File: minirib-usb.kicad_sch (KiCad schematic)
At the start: 53 parts, among them J1 USB_B_Micro, J2 SB9600 Out, Q1 MMST3904-7-F, Q2 MMST3906-7-F, Q3 MMST3906-7-F, Q4 MMST3904-7-F, Q5 MMST3904-7-F, Q6 MMST3904-7-F, Q7 MMST3904-7-F, Q8 MMST3906-7-F, Q9 MMST3906-7-F, U1 CH340G, U2 MCP6491T-E, Y1 12MHz

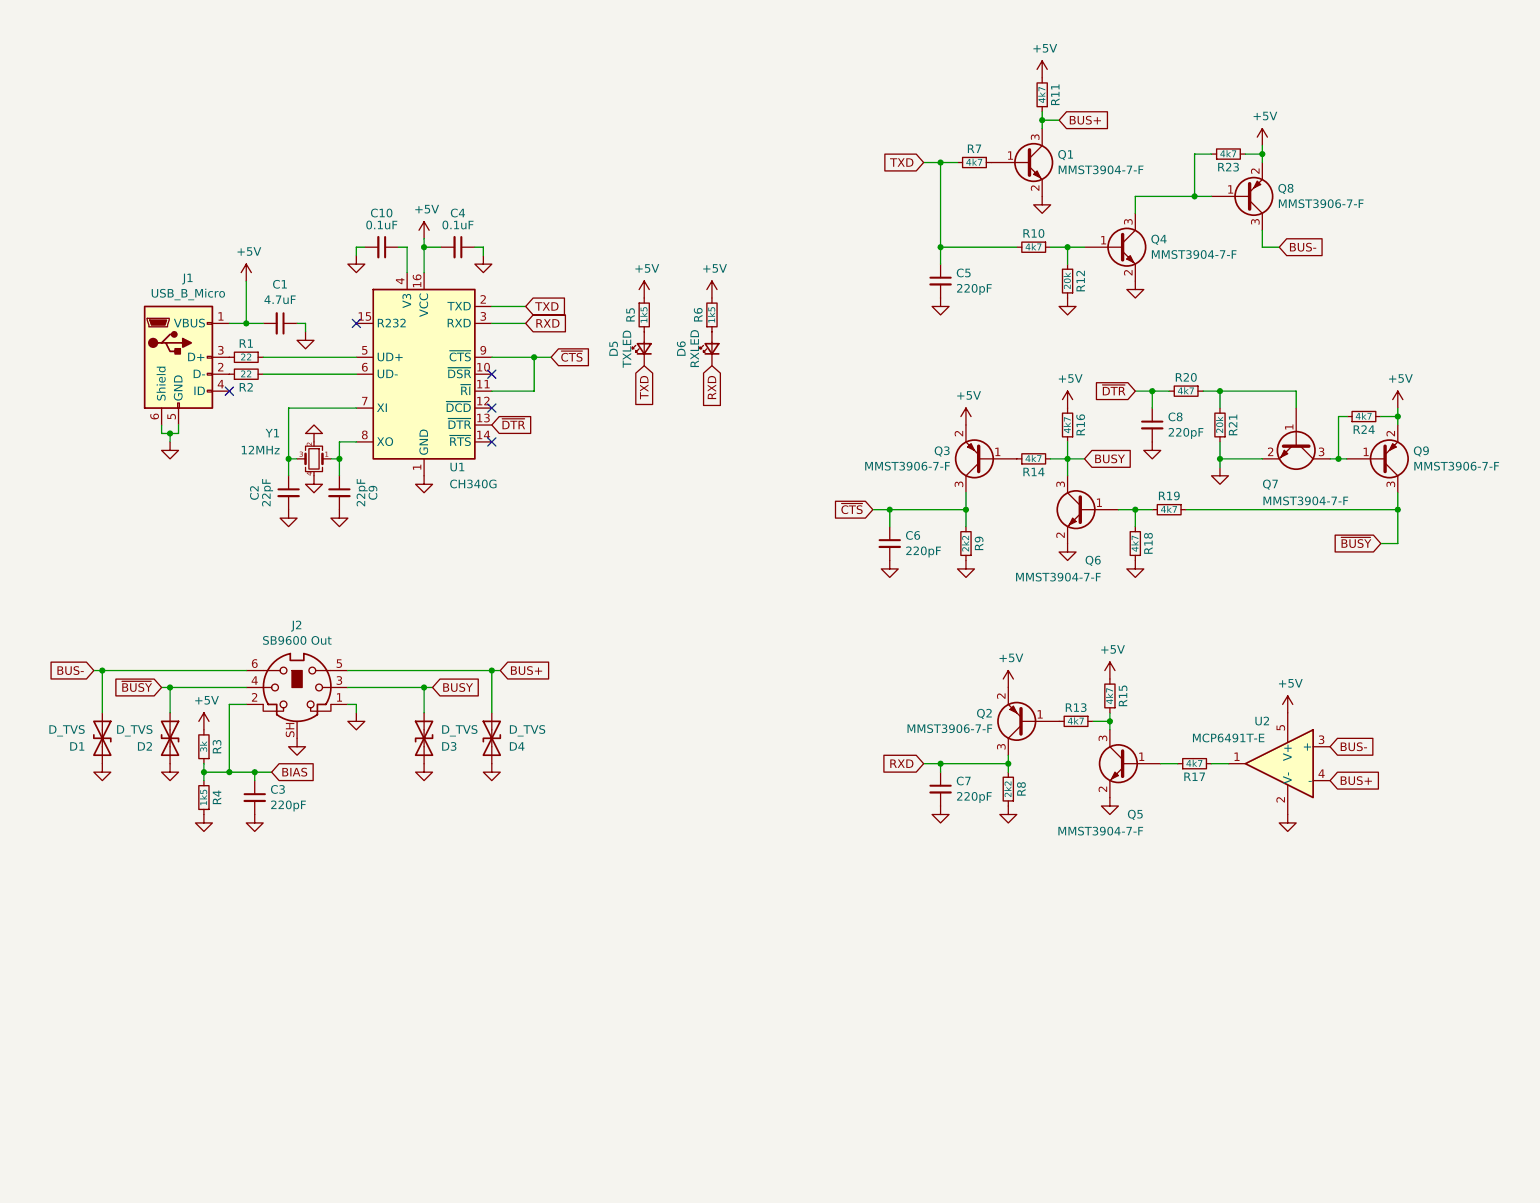
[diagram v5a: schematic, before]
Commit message: rev C total redesign
Changed circuit to use an FT231 + MAX232 usb chain, with original transistor logic conversion identical to the RLN4008B schematic to ensure proper operation
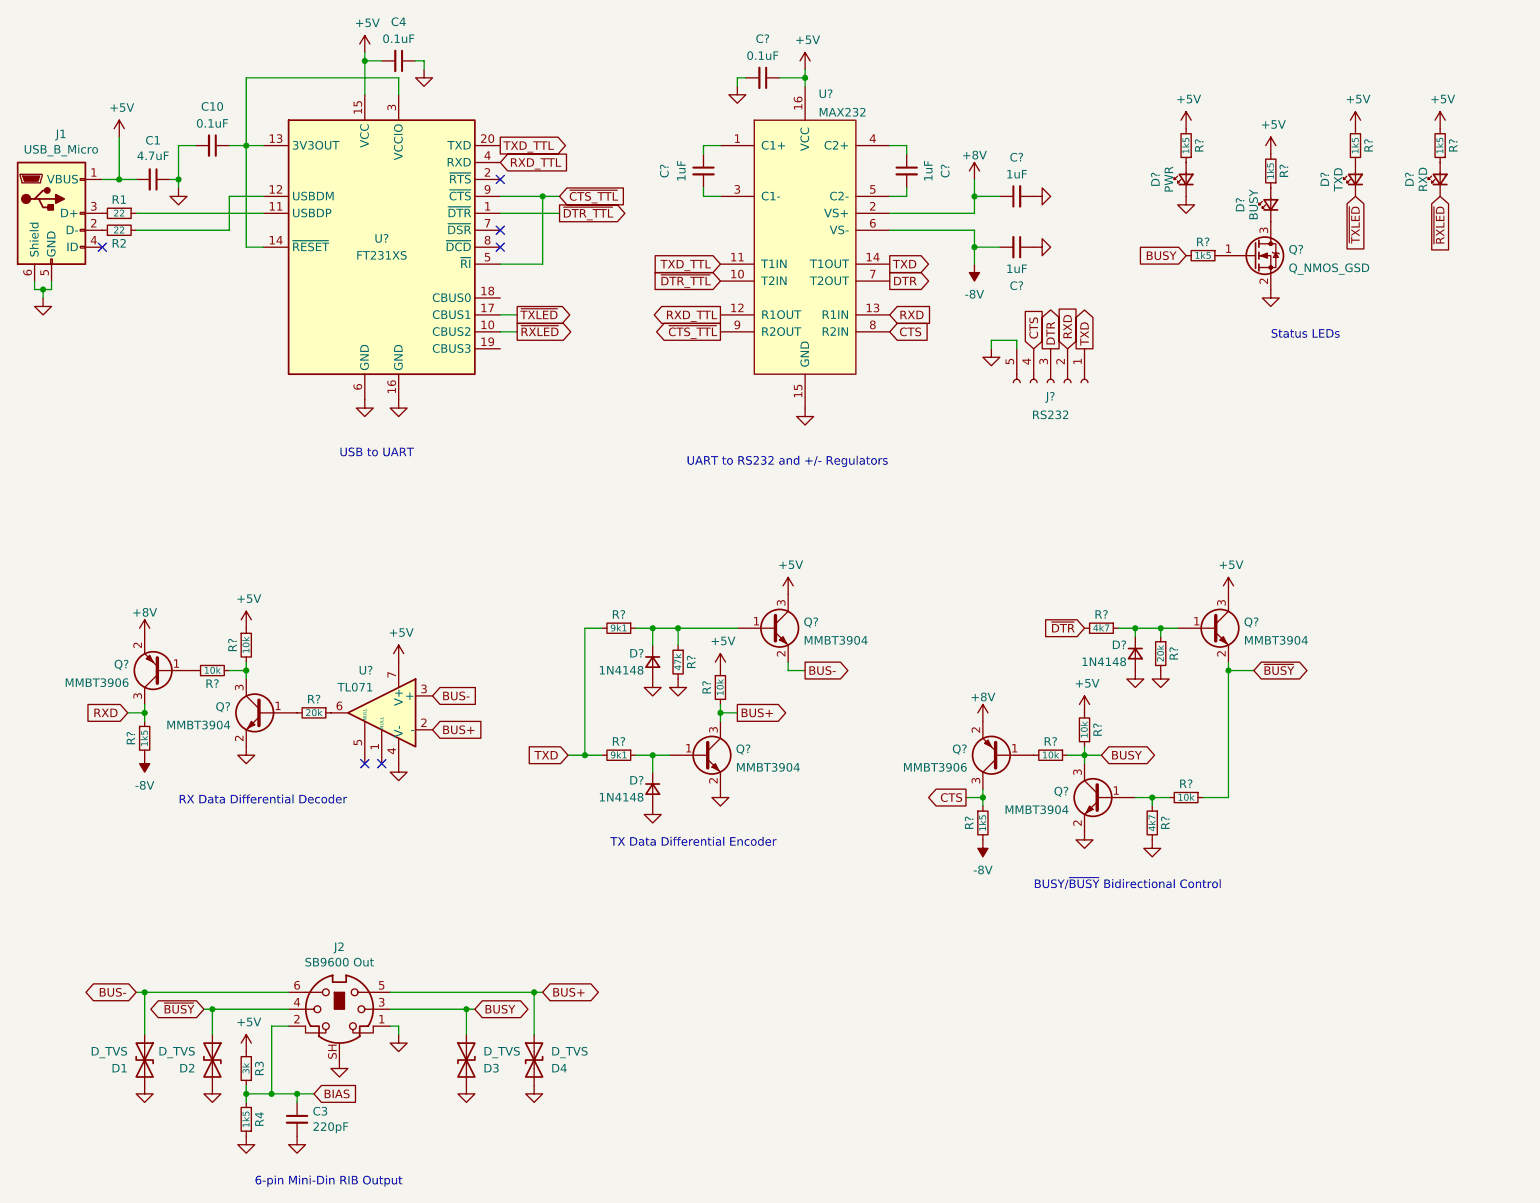
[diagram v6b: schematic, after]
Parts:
- removed C2, C9: 22pF, Capacitor_SMD:C_0805_2012Metric_Pad1.18x1.45mm_HandSolder, symbol Device:C_Small
- removed C5, C6, C7, C8: 220pF, Capacitor_SMD:C_0805_2012Metric_Pad1.18x1.45mm_HandSolder, symbol Device:C_Small
- removed D5: TXLED, Diode_SMD:D_0805_2012Metric_Pad1.15x1.40mm_HandSolder, symbol Device:LED_Small
- removed D6: RXLED, Diode_SMD:D_0805_2012Metric_Pad1.15x1.40mm_HandSolder, symbol Device:LED_Small
- removed Q1, Q4, Q5, Q6, Q7: MMST3904-7-F, Package_TO_SOT_SMD:SOT-323_SC-70_Handsoldering, symbol Device:Q_NPN_BEC
- removed Q2, Q3, Q8, Q9: MMST3906-7-F, Package_TO_SOT_SMD:SOT-323_SC-70_Handsoldering, symbol Device:Q_PNP_BEC
- removed R10, R11, R13, R14, R15, R16, R17, R18, R19, R20, R23, R24, R7: 4k7, Resistor_SMD:R_0805_2012Metric_Pad1.20x1.40mm_HandSolder, symbol Device:R_Small
- removed R12, R21: 20k, Resistor_SMD:R_0805_2012Metric_Pad1.20x1.40mm_HandSolder, symbol Device:R_Small
- removed R5, R6: 1k5, Resistor_SMD:R_0805_2012Metric_Pad1.20x1.40mm_HandSolder, symbol Device:R_Small
- removed R8, R9: 2k2, Resistor_SMD:R_0805_2012Metric_Pad1.20x1.40mm_HandSolder, symbol Device:R_Small
- removed U1: CH340G, Package_SO:SOIC-16_3.9x9.9mm_P1.27mm, symbol Interface_USB:CH340G
- removed U2: MCP6491T-E, Package_TO_SOT_SMD:SOT-353_SC-70-5_Handsoldering, symbol MiniDin:TL081H
- removed Y1: 12MHz, Crystal:Crystal_SMD_SeikoEpson_FA238-4Pin_3.2x2.5mm_HandSoldering, symbol Device:Crystal_GND24_Small
- added C? (x4): 1uF, Capacitor_SMD:C_0805_2012Metric_Pad1.18x1.45mm_HandSolder, symbol Device:C_Small
- added C?: 0.1uF, Capacitor_SMD:C_0805_2012Metric_Pad1.18x1.45mm_HandSolder, symbol Device:C_Small
- added D?: PWR, Diode_SMD:D_0805_2012Metric_Pad1.15x1.40mm_HandSolder, symbol Device:LED_Small
- added D?: TXD, Diode_SMD:D_0805_2012Metric_Pad1.15x1.40mm_HandSolder, symbol Device:LED_Small
- added D? (x3): 1N4148, symbol Device:D_Small
- added D?: BUSY, Diode_SMD:D_0805_2012Metric_Pad1.15x1.40mm_HandSolder, symbol Device:LED_Small
- added D?: RXD, Diode_SMD:D_0805_2012Metric_Pad1.15x1.40mm_HandSolder, symbol Device:LED_Small
- added J?: RS232, symbol Connector:Conn_01x05_Female
- added Q? (x5): MMBT3904, Package_TO_SOT_SMD:SOT-23, symbol Transistor_BJT:MMBT3904
- added Q?: Q_NMOS_GSD, symbol Device:Q_NMOS_GSD
- added Q? (x2): MMBT3906, Package_TO_SOT_SMD:SOT-23, symbol Transistor_BJT:MMBT3906
- added R? (x7): 1k5, Resistor_SMD:R_0805_2012Metric_Pad1.20x1.40mm_HandSolder, symbol Device:R_Small
- added R? (x6): 10k, Resistor_SMD:R_0805_2012Metric_Pad1.20x1.40mm_HandSolder, symbol Device:R_Small
- added R?: 47k, Resistor_SMD:R_0805_2012Metric_Pad1.20x1.40mm_HandSolder, symbol Device:R_Small
- added R? (x2): 9k1, Resistor_SMD:R_0805_2012Metric_Pad1.20x1.40mm_HandSolder, symbol Device:R_Small
- added R? (x2): 4k7, Resistor_SMD:R_0805_2012Metric_Pad1.20x1.40mm_HandSolder, symbol Device:R_Small
- added R? (x2): 20k, Resistor_SMD:R_0805_2012Metric_Pad1.20x1.40mm_HandSolder, symbol Device:R_Small
- added U?: FT231XS, Package_SO:SSOP-20_3.9x8.7mm_P0.635mm, symbol Interface_USB:FT231XS
- added U?: MAX232, symbol max232:MAX232
- added U?: TL071, symbol Amplifier_Operational:TL071
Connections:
- net +5V: now also C?.1, Q?.3 (C), Q?.3 (C), R?.1, R?.1, R?.2, R?.2, R?.2, R?.2, R?.2, U?.15 (VCC), U?.16 (VCC), U?.7 (V+)
- net BUS+: now also Q?.3 (C), R?.2, U?.2 (-)
- net BUS-: now also Q?.2 (E), U?.3 (+)
- net BUSY: now also Q?.3 (C), R?.1, R?.1, R?.2
- net GND: now also C?.1, C?.2, C?.2, D?.1 (K), D?.2 (A), D?.2 (A), D?.2 (A), J?.5 (Pin_5), Q?.2 (E), Q?.2 (E), Q?.2 (E), Q?.2 (S), R?.2, R?.2, R?.2, U?.15 (GND), U?.16 (GND), U?.4 (V-), U?.6 (GND)
- net RXD: now also J?.2 (Pin_2), Q?.3 (C), R?.1, U?.13 (R1IN)
- net TXD: now also J?.1 (Pin_1), R?.2, R?.2, U?.14 (T1OUT)
- net ~{BUSY}: now also Q?.2 (E), R?.1
- net ~{DTR}: now also R?.2
- net at R1.1: now also U?.11 (USBDP)
- net at R2.2: now also U?.12 (USBDM)
- net at C10.1: now also U?.13 (3V3OUT), U?.14 (~{RESET}), U?.3 (VCCIO)
- new net: Q?.1 (G), R?.1
- new net: D?.2 (A), R?.1 (x4)
- new net: D?.1 (K), Q?.1 (B), R?.1, R?.1 (x2)
- new net: Q?.1 (B), R?.2 (x2)
- new net: Q?.1 (B), R?.1, R?.2
- new net: Q?.3 (C), R?.2, R?.2
- new net: D?.1 (K), Q?.3 (D)
- new net: Q?.1 (B), R?.1
- new net: C?.1, U?.1 (C1+)
- new net: C?.2, U?.3 (C1-)
- new net: C?.1, U?.4 (C2+)
- new net: C?.2, U?.5 (C2-)
- new net: D?.1 (K), Q?.1 (B), R?.1
- new net: R?.1, U?.6
- new net +8V: C?.1, Q?.2 (E), Q?.2 (E), U?.2 (VS+)
- new net -8V: C?.2, R?.2, R?.2, U?.6 (VS-)
- new net CTS: J?.4 (Pin_4), Q?.3 (C), R?.1, U?.8 (R2IN)
- new net DTR: J?.3 (Pin_3), U?.7 (T2OUT)
- new net RXD_TTL: U?.12 (R1OUT), U?.4 (RXD)
- new net TXD_TTL: U?.11 (T1IN), U?.20 (TXD)
- new net ~{CTS_TTL}: U?.5 (~{RI}), U?.9 (R2OUT), U?.9 (~{CTS})
- new net ~{DTR_TTL}: U?.1 (~{DTR}), U?.10 (T2IN)
- new net ~{RXLED}: D?.1 (K), U?.10 (CBUS2)
- new net ~{TXLED}: D?.1 (K), U?.17 (CBUS1)
- no-connect marks 5 -> 6
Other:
- note added: "6-pin Mini-Din RIB Output"
- note added: "BUSY/~{BUSY} Bidirectional Control"
- note added: "RX Data Differential Decoder"
- note added: "Status LEDs"
- note added: "TX Data Differential Encoder"
- note added: "UART to RS232 and +/- Regulators"
- note added: "USB to UART"
- moved on the sheet: C1, C10, C3, C4, D1, D2, D3, D4, J1, J2, R1, R2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

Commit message: finalized schematic and pcb
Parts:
- removed R3: 3k, Resistor_SMD:R_0805_2012Metric_Pad1.20x1.40mm_HandSolder, symbol Device:R_Small
- removed R4: 1k5, Resistor_SMD:R_0805_2012Metric_Pad1.20x1.40mm_HandSolder, symbol Device:R_Small
- removed U?: TL071, symbol Amplifier_Operational:TL071
- added C6: 1uF, Capacitor_SMD:C_0805_2012Metric_Pad1.18x1.45mm_HandSolder, symbol Device:C_Small
- added R6: 39k, Resistor_SMD:R_0805_2012Metric_Pad1.20x1.40mm_HandSolder, symbol Device:R_Small
- added R7: 10k, Resistor_SMD:R_0805_2012Metric_Pad1.20x1.40mm_HandSolder, symbol Device:R_Small
- added U2: TL071, Package_TO_SOT_SMD:SOT-23-5_HandSoldering, symbol MiniDin:TL071
- D5, D6, D7: renamed from D?; footprint (none) -> Diode_SMD:D_SOD-323_HandSoldering
- J2: value SB9600 Out -> Mini-DIN-6-Shielded
- J3: renamed from J?; footprint (none) -> Connector_PinHeader_1.27mm:PinHeader_1x05_P1.27mm_Vertical
- Q8: renamed from Q?; value Q_NMOS_GSD -> BSS138W; footprint (none) -> Package_TO_SOT_SMD:SOT-323_SC-70_Handsoldering
- U3: renamed from U?; footprint (none) -> Package_SO:SOIC-16W_7.5x10.3mm_P1.27mm
- gave numbers to parts that had none: 37
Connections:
- net ~{DTR} is gone; now on net DTR: R16.2
- net +5V: now also C6.1, R6.1, U2.5 (V+)
- net BIAS: now also R6.2, R7.1
- net BUS+: now also U2.4 (-)
- net BUS-: now also U2.3 (+)
- net GND: now also C6.2, R7.2, U2.2 (V-)
- net at R8.1: now also U2.1

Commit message: generated schematic and gerbers for rev C PCB
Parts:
- J3: footprint Connector_PinHeader_1.27mm:PinHeader_1x05_P1.27mm_Vertical -> Connector_PinHeader_2.54mm:PinHeader_1x05_P2.54mm_Vertical
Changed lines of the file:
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@@
   (title_block
     (title "MiniRIB-USB")
-    (date "2022-05-05")
+    (date "2022-10-12")
     (rev "C")
     (company "W3AXL")
@@
     (property "Reference" "J3" (id 0) (at 189.23 79.5687 90))
     (property "Value" "RS232" (id 1) (at 189.23 82.3438 90))
-    (property "Footprint" "Connector_PinHeader_1.27mm:PinHeader_1x05_P1.27mm_Vertical" (id 2) (at 189.23 77.47 0)
+    (property "Footprint" "Connector_PinHeader_2.54mm:PinHeader_1x05_P2.54mm_Vertical" (id 2) (at 189.23 77.47 0)
       (effects (font (size 1.27 1.27)) hide)
     )
@@
     )
     (path "/55a317c2-22a5-4365-8e54-bca6e8c5492e"
-      (reference "J3") (unit 1) (value "RS232") (footprint "Connector_PinHeader_1.27mm:PinHeader_1x05_P1.27mm_Vertical")
+      (reference "J3") (unit 1) (value "RS232") (footprint "Connector_PinHeader_2.54mm:PinHeader_1x05_P2.54mm_Vertical")
     )
     (path "/af5c60b5-8759-4955-8681-0d321320f557"
